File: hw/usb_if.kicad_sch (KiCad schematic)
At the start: 20 parts, among them J2 USB_C_Receptacle_USB2.0, U16 USB3343

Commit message: WIP - a lot already laid out.
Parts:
- removed C100: 100n, Capacitor_SMD:C_0603_1608Metric, symbol fmc:100nF_603
- removed R? (x4): 10k, Resistor_SMD:R_0603_1608Metric, symbol Device:R_Small
- removed R?: 5k1, Resistor_SMD:R_0603_1608Metric, symbol Device:R_Small
- removed R?: 35k7, Resistor_SMD:R_0603_1608Metric, symbol Device:R_Small
- removed U?: UTC2000, Package_DFN_QFN:QFN-16-1EP_3x3mm_P0.5mm_EP1.75x1.75mm_ThermalVias, symbol fmc:UTC2000
- added R?: 0, Resistor_SMD:R_0603_1608Metric, symbol Device:R_Small
- J2: footprint proj_footprints:USB_C_Receptacle_GCT_USB4085_smaller_holes -> proj_footprints:USB_C_Receptacle_Molex_2171790001_16P_TopMnt_Horizontal; Manufacturer (none) -> Molex; Part (none) -> 2171790001
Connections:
- net ULPI_RSTb: now also R?.1; no longer R?.2, U16.22 (~{RESETB})
- new net: R?.2, R?.2, U16.22 (~{RESETB})
- no-connect marks 10 -> 3

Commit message: finished routing; DRC passes (except for 1 hole violation at push-button)
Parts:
- C100: Manufacturer Murata -> (none); Part GCJ188R71E104KA12D -> (none)
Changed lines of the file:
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@@
       (effects (font (size 1.27 1.27)) hide)
     )
-    (property "Part" "GCJ188R71E104KA12D" (at 42.545 95.25 0)
-      (effects (font (size 1.27 1.27)) hide)
-    )
-    (property "Manufacturer" "Murata" (at 40.005 92.71 0)
+    (property "Part" "" (at 42.545 95.25 0)
+      (effects (font (size 1.27 1.27)) hide)
+    )
+    (property "Manufacturer" "" (at 40.005 92.71 0)
       (effects (font (size 1.27 1.27)) hide)
     )
@@
       (effects (font (size 1.27 1.27)) hide)
     )
-    (property "Part" "GCJ188R71E104KA12D" (at 168.275 41.91 0)
-      (effects (font (size 1.27 1.27)) hide)
-    )
-    (property "Manufacturer" "Murata" (at 170.815 39.37 0)
+    (property "Part" "" (at 168.275 41.91 0)
+      (effects (font (size 1.27 1.27)) hide)
+    )
+    (property "Manufacturer" "" (at 170.815 39.37 0)
       (effects (font (size 1.27 1.27)) hide)
     )
@@
       (effects (font (size 1.27 1.27)) hide)
     )
-    (property "Part" "GCJ188R71E104KA12D" (at 130.175 57.15 0)
-      (effects (font (size 1.27 1.27)) hide)
-    )
-    (property "Manufacturer" "Murata" (at 132.715 54.61 0)
-      (effects (font (size 1.27 1.27)) hide)
-    )
+    (property "Part" "" (at 130.175 57.15 0)
+      (effects (font (size 1.27 1.27)) hide)
+    )
+    (property "Manufacturer" "" (at 132.715 54.61 0)
+      (effects (font (size 1.27 1.27)) hide)
+    )

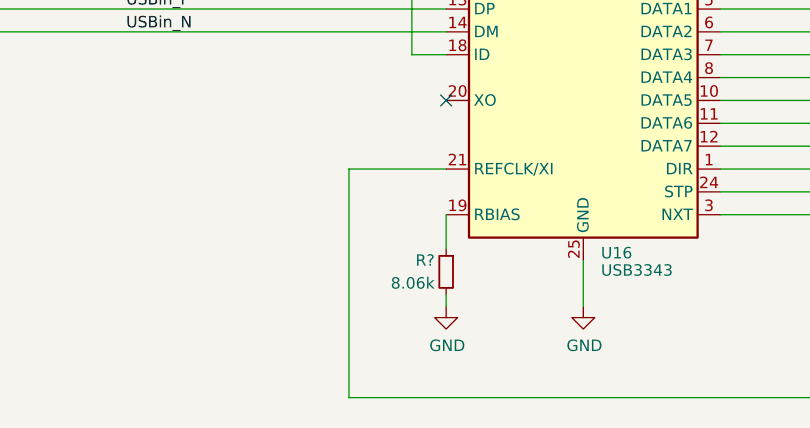
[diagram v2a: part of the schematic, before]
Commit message: standardized resistor/capacitor values
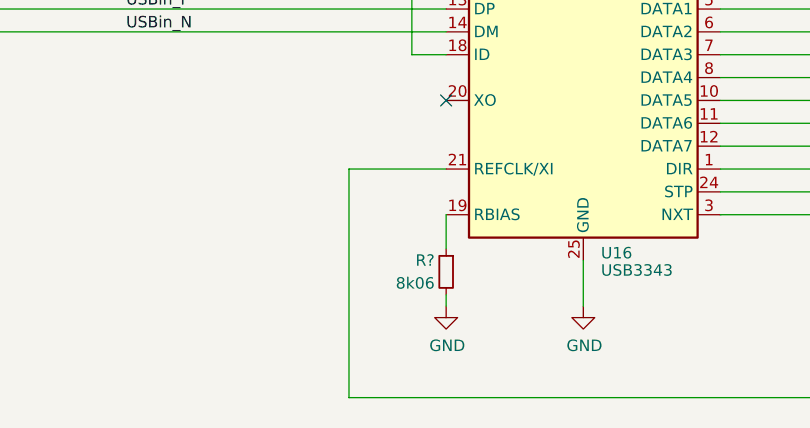
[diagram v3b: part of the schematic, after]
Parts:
- R?: value 8.06k -> 8k06
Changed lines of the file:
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@@
       (effects (font (size 1.27 1.27)) (justify left))
     )
-    (property "Value" "8.06k" (at 140.97 110.49 0)
+    (property "Value" "8k06" (at 140.97 110.49 0)
       (effects (font (size 1.27 1.27)) (justify left))
     )

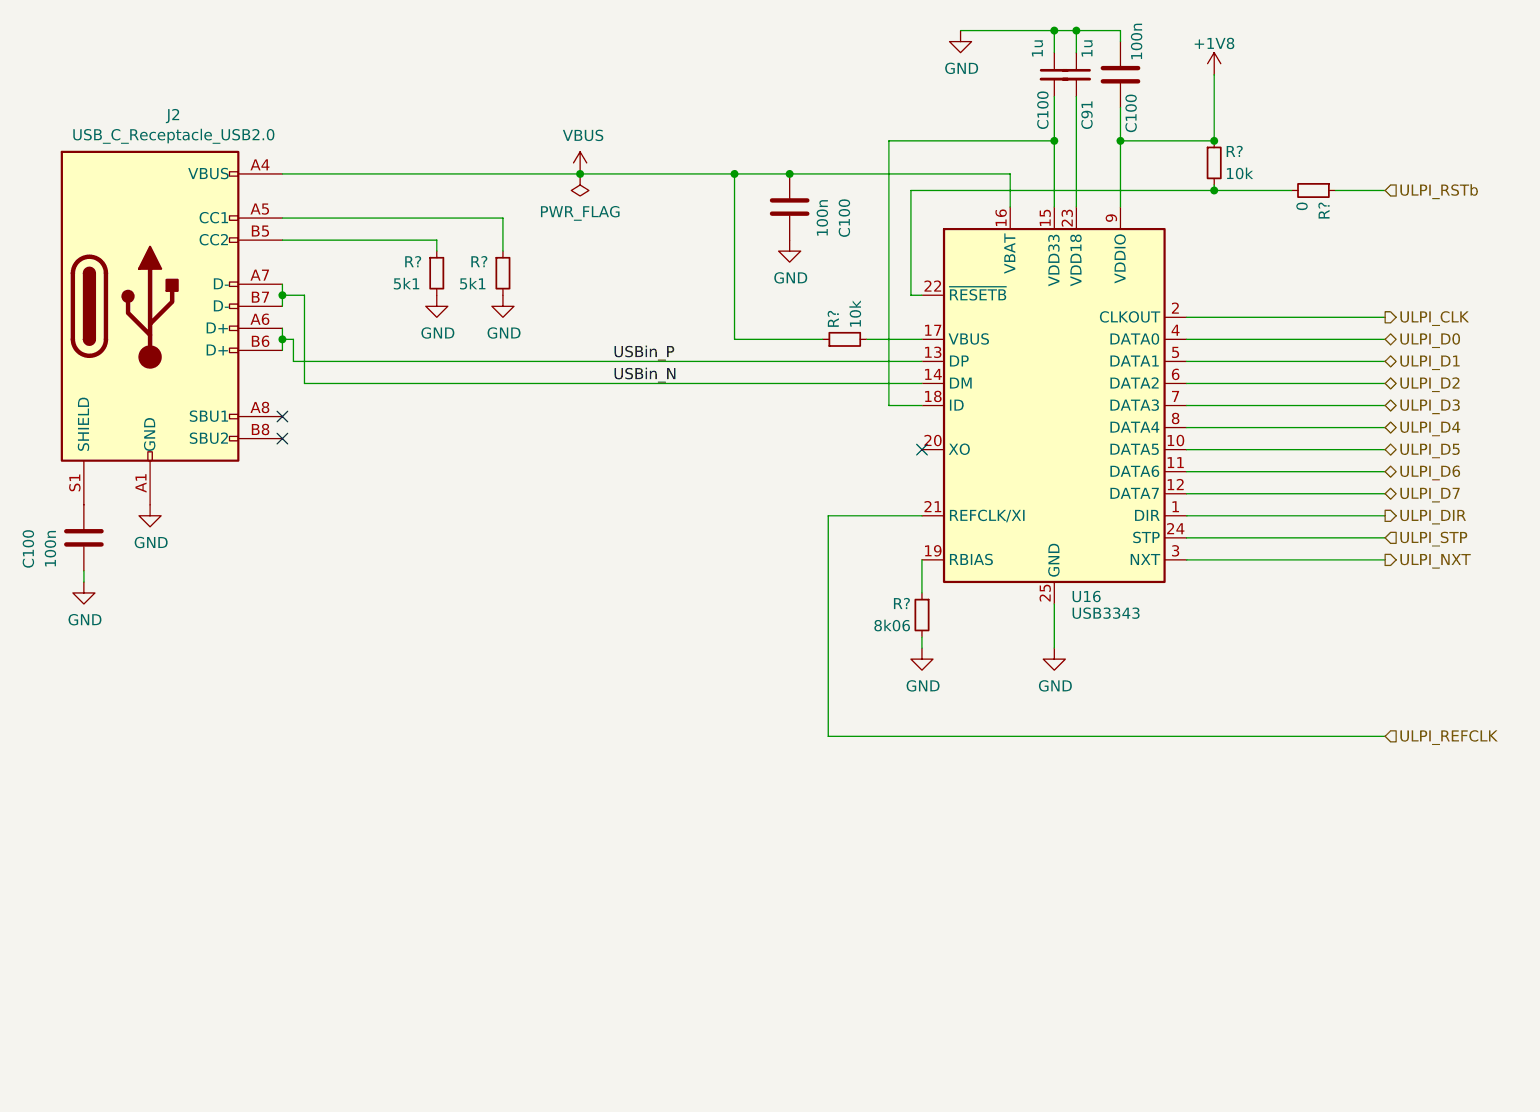
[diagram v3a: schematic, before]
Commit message: Added trion top-sheet as sub-sheet to usbadc project
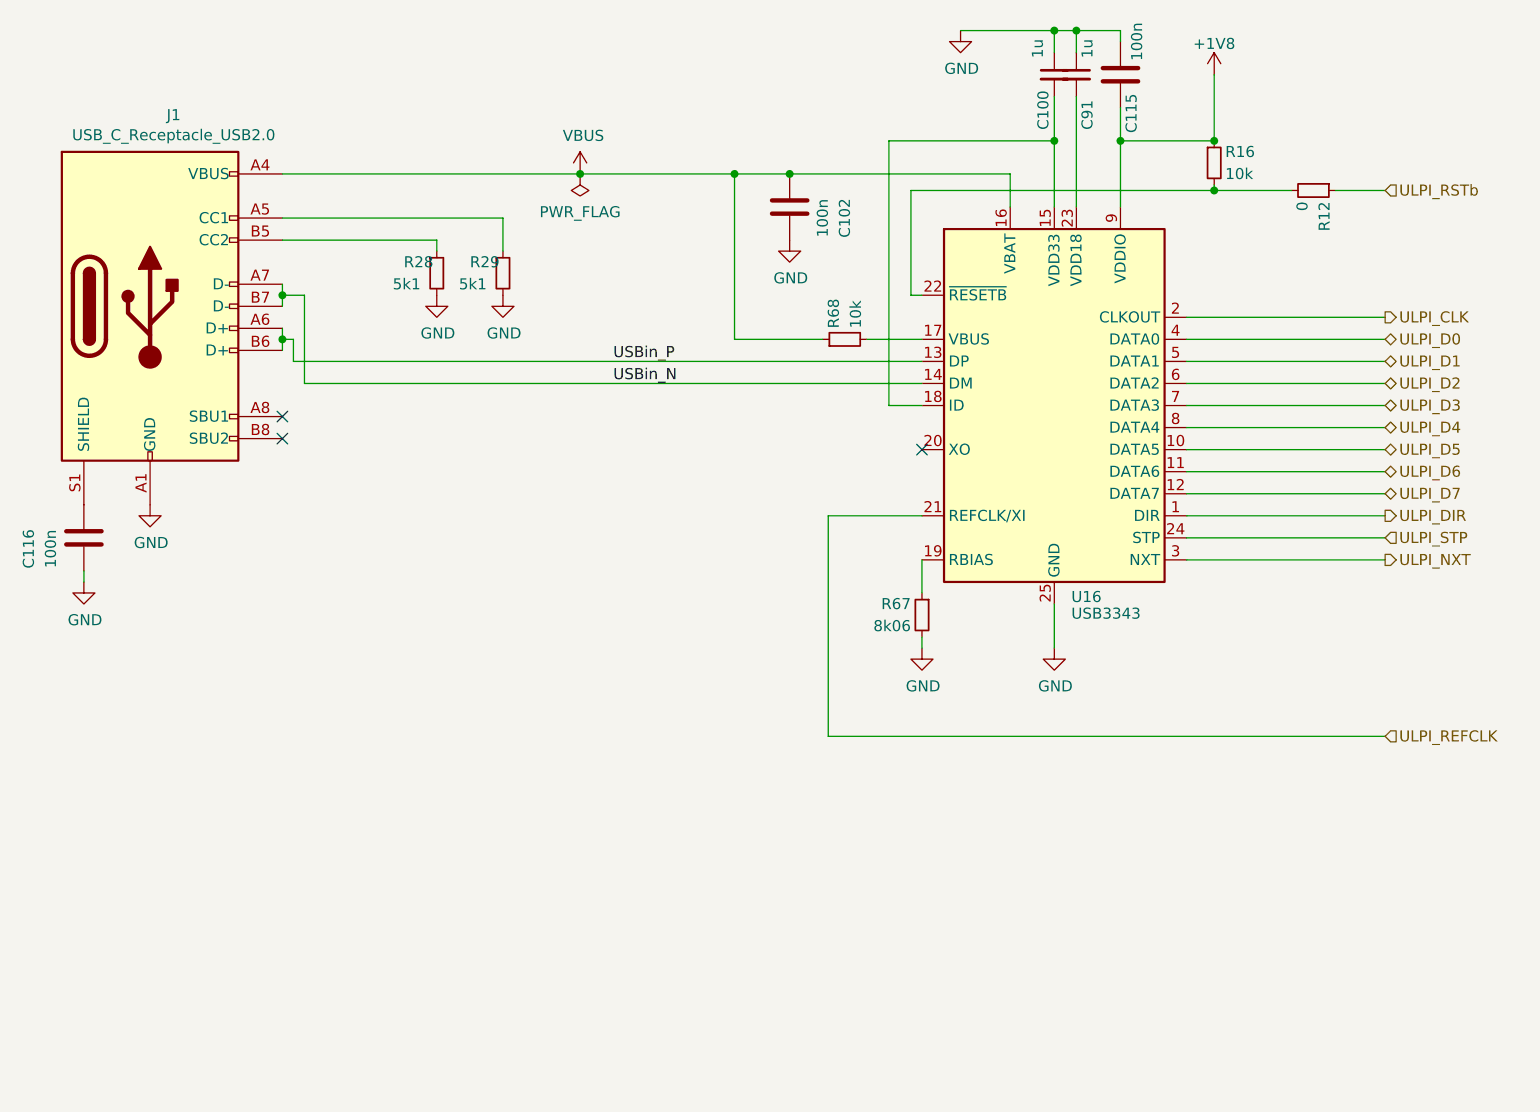
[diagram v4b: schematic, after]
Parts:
- gave numbers to parts that had none: 6
- renumbered C100 to C102, C100 to C115, C100 to C116, J2 to J1

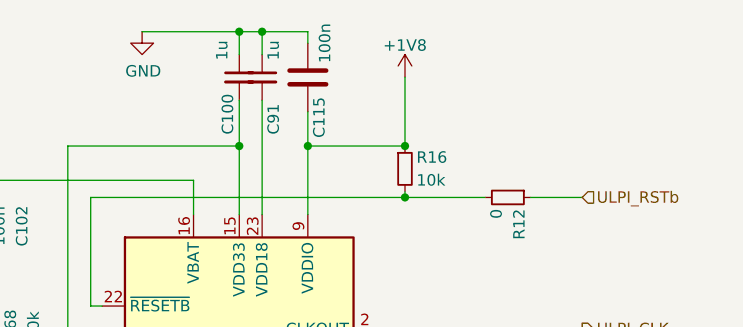
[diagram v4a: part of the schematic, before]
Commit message: moved trion into place; going to 'hide' footprint reference designators...
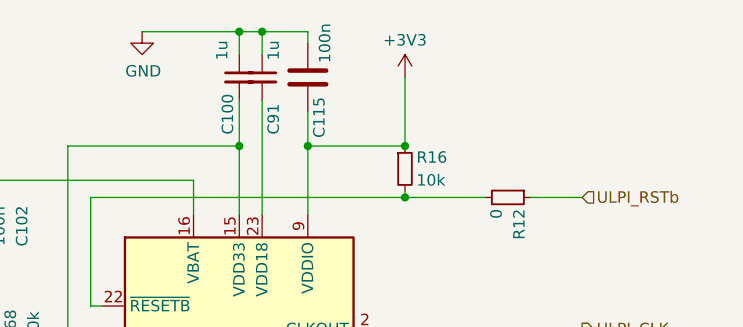
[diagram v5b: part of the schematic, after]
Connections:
- net +1V8 renamed +3V3
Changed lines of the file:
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@@
-    )
-  )
-  (symbol (lib_id "power:+1V8") (at 175.895 46.99 0) (unit 1)
-    (in_bom yes) (on_board yes) (dnp no)
-    (property "Reference" "#PWR085" (at 175.895 50.8 0)
-      (effects (font (size 1.27 1.27)) hide)
-    )
-    (property "Value" "+1V8" (at 175.895 43.434 0)
-      (effects (font (size 1.27 1.27)))
-    )
-    (property "Footprint" "" (at 175.895 46.99 0)
-      (effects (font (size 1.27 1.27)) hide)
-    )
-    (property "Datasheet" "" (at 175.895 46.99 0)
-      (effects (font (size 1.27 1.27)) hide)
-    )
-    (pin "1")
-    (instances
-      (project "usbadc"
-        (path "/7c8a1f8d-8834-4c9b-aaae-1f231e9b09a1/5598a6a2-be47-454c-8f97-749ceb56c3dc"
-          (reference "#PWR085") (unit 1)
-        )
-      )
     )
   )
@@
         )
       )
+    )
+  )
+  (symbol (lib_id "power:+3V3") (at 175.895 46.99 0) (unit 1)
+    (in_bom yes) (on_board yes) (dnp no) (fields_autoplaced)
+    (property "Reference" "#PWR085" (at 175.895 50.8 0)
+      (effects (font (size 1.27 1.27)) hide)
+    )
+    (property "Value" "+3V3" (at 175.895 42.8569 0)
+      (effects (font (size 1.27 1.27)))
+    )
+    (property "Footprint" "" (at 175.895 46.99 0)
+      (effects (font (size 1.27 1.27)) hide)
+    )
+    (property "Datasheet" "" (at 175.895 46.99 0)
+      (effects (font (size 1.27 1.27)) hide)
+    )
+    (pin "1")
+    (instances
+      (project "usbadc"
+        (path "/7c8a1f8d-8834-4c9b-aaae-1f231e9b09a1/5598a6a2-be47-454c-8f97-749ceb56c3dc"
+          (reference "#PWR085") (unit 1)
+        )
+      )

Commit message: finalizing...
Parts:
- J1: symbol Connector:USB_C_Receptacle_USB2.0 -> Connector:USB_C_Receptacle_USB2.0_16P
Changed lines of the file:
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@@
     )
   )
-  (symbol (lib_id "Connector:USB_C_Receptacle_USB2.0") (at 53.34 73.66 0) (unit 1)
+  (symbol (lib_id "Connector:USB_C_Receptacle_USB2.0_16P") (at 53.34 73.66 0) (unit 1)
     (in_bom yes) (on_board yes) (dnp no)
     (property "Reference" "J1" (at 56.0578 51.6382 0)
